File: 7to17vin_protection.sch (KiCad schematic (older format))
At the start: 10 parts

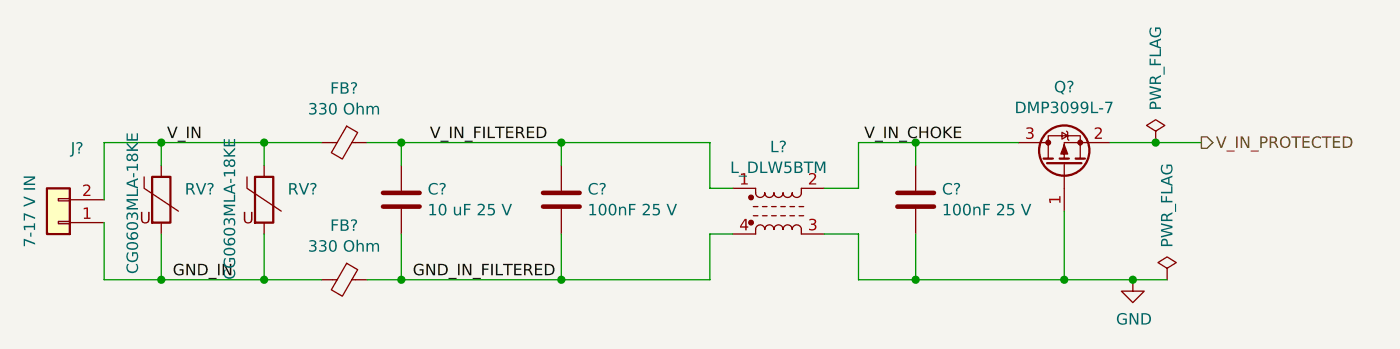
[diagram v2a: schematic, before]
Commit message: Schematic modified (Hierarchy) Bug where SPI was active when creset or ss was low fixed PCB layout started (almost all parts are at position) No parts on the bottom so far Arduino and PMOD header spacings corrected according to its standards
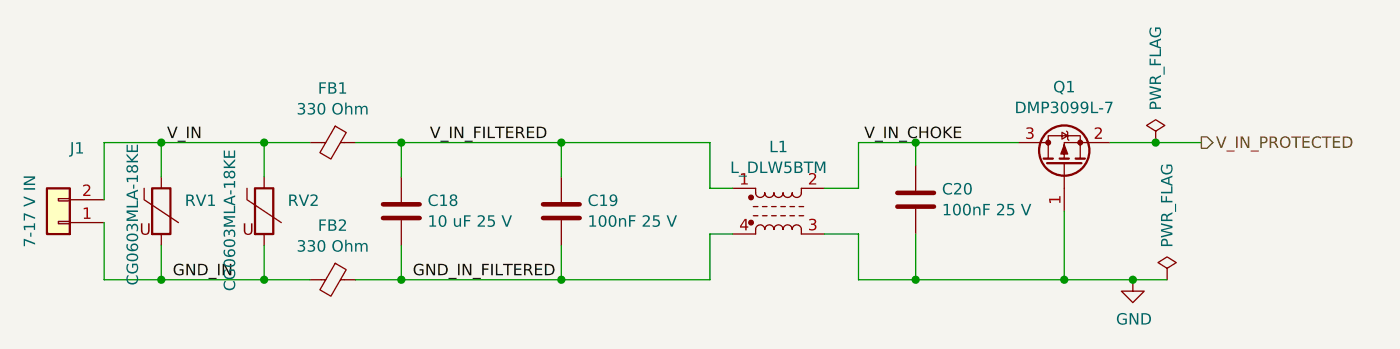
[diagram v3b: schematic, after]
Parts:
- gave numbers to parts that had none: 10
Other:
- moved on the sheet: C18, C19, FB1, FB2, RV1, RV2
